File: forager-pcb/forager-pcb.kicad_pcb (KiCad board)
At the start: 2 copper layers, 236.5 x 96.3 mm, 90 parts, among them J1 Conn_01x02_Pin, J2 Conn_01x02_Pin

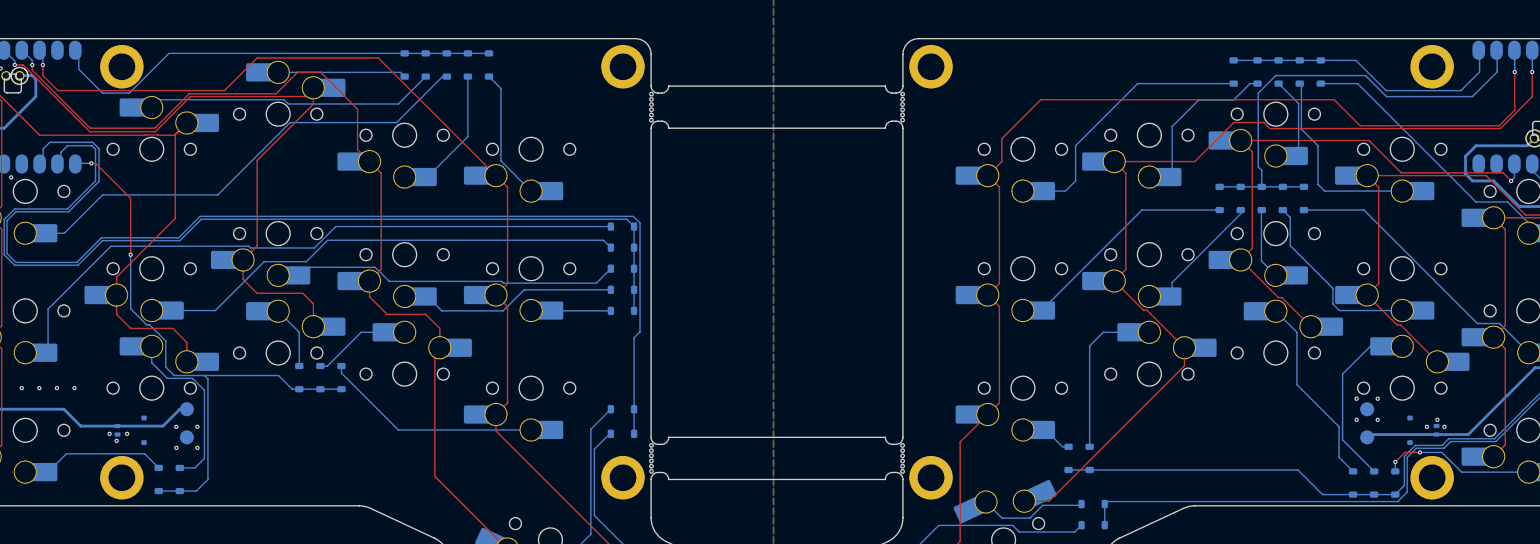
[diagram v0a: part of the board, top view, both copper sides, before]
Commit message: kicad: add antenna keepout zone
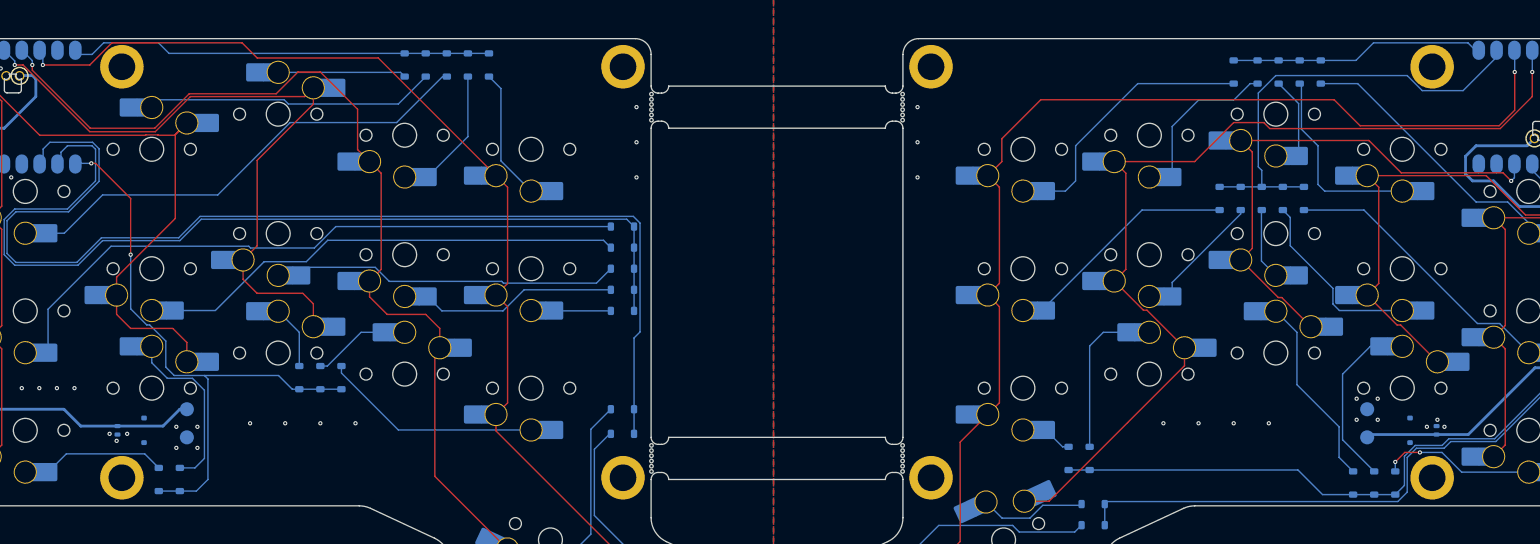
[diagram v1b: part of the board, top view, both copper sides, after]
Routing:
- net /LROW0: track 64.4 -> 60.2 mm
- net /RROW0: track 40.1 -> 36.5 mm
- net /LCOL4: track 155.4 -> 153.3 mm
- net /RROW1: track 65.5 -> 63.5 mm
- net RGND: vias 11 -> 18
- net LGND: vias 21 -> 28
